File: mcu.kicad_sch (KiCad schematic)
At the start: 32 parts, among them J1 FTSH-105-01-F-DV-P-TR, J5 2337019-1, SW1 SW_Push, U1 nRF52840, U5 MX25R6435FZAIL0, U6 AP22814AW5, Y1 32MHz, Y2 32.768kHz

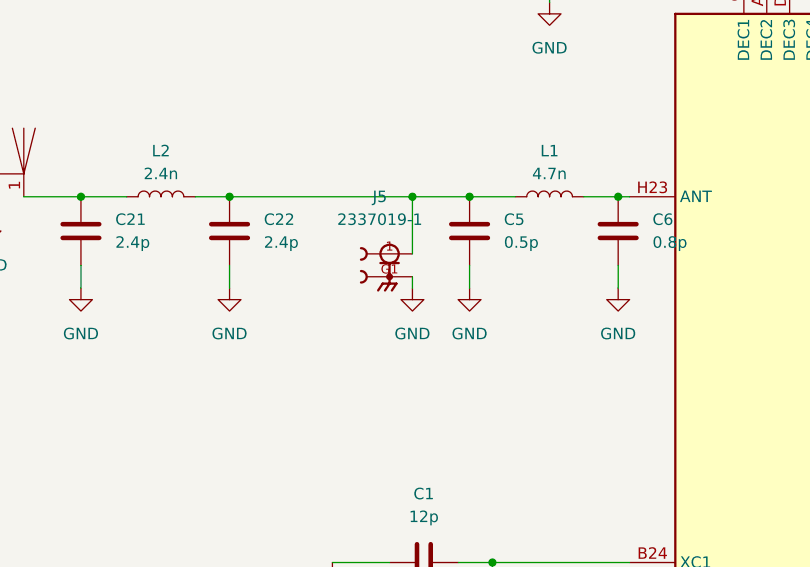
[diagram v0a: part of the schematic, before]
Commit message: Added mounting holes and other final touches
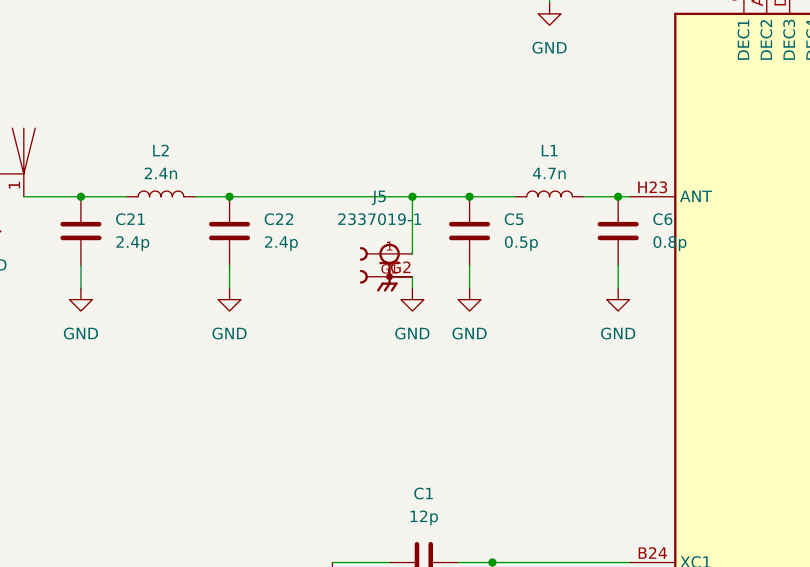
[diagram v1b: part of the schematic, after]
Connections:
- net GND: now also J5.G2
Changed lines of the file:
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@@
 	(wire
 		(pts
+			(xy 68.58 62.23) (xy 68.58 63.5)
+		)
+		(stroke
+			(width 0)
+			(type default)
+		)
+	)
+	(wire
+		(pts
 			(xy 31.75 142.24) (xy 40.64 142.24)
 		)
@@
 	(wire
 		(pts
-			(xy 68.58 62.23) (xy 68.58 63.5)
-		)
-		(stroke
-			(width 0)
-			(type default)
-		)
-	)
-	(wire
-		(pts
 			(xy 172.72 105.41) (xy 204.47 105.41)
 		)
@@
 		(pin "1"
 		)
+		(pin "G2"
+		)
 		(instances
 			(project ""
@@
 		(lib_id "power:GND")
 		(at 68.58 63.5 0)
+		(mirror y)
 		(unit 1)
 		(exclude_from_sim no)
@@
 		(on_board yes)
 		(dnp no)
-		(fields_autoplaced yes)
 		(property "Reference" "#PWR057"
 			(at 68.58 69.85 0)

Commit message: Made modifications from fabrication
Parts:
- C1, C2, C3, C4: MPN (none) -> C107034
- C11, C17, C25: MPN (none) -> C15849
- C12, C13, C16: MPN (none) -> C14663
- C14, C15: MPN (none) -> C19666
- C18: MPN (none) -> C14665
- C21, C22: MPN (none) -> C710896
- C5: MPN (none) -> C162254
- C6: MPN (none) -> C907996
- J1: MPN (none) -> C5136979
- J5: MPN (none) -> C434807
- L1: MPN (none) -> C98078
- L2: MPN (none) -> C2042508
- R10, R11, R12: MPN (none) -> C98220
- R13: MPN (none) -> C14675
- U1: MPN (none) -> C190794
- U5: MPN (none) -> C2802847
- U6: MPN (none) -> C2680321
- Y1: MPN (none) -> C5265796
- Y2: LCSC PN C7496559 -> C32346; MPN (none) -> C32346; Part Number DH2032K768C5T8188001 -> Q13FC13500004
